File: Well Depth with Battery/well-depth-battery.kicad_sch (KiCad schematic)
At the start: 59 parts, among them J1 Conn_01x02_Female, J2 Conn_01x04_Female, J3 Conn_01x04_Male, J4 Conn_01x02_Male, J5 USB_A, Q1 Q_NMOS_GSD, Q2 Q_PMOS_GSD, Q3 Q_PMOS_GSD, U1 LM358, U2 LM358, U3 TL431DBZ, U4 PCF85263AT, U5 ATSAMD11C14A-SS, U6 MCP1793T-3302H/DC, Y1 Crystal_Small

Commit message: WDB: Floorplanning
Also fixed .gitignore to not ignore lib
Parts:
- removed H4: MountingHole, MountingHole:MountingHole_3.2mm_M3, symbol Mechanical:MountingHole
- J5: footprint Connector_USB:USB_A_Molex_67643_Horizontal -> Connector_USB:USB_A_Molex_105057_Vertical
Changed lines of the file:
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@@
     (pin "2")
-  )
-  (symbol (lib_id "Mechanical:MountingHole") (at 140.97 39.37 0) (unit 1)
-    (in_bom yes) (on_board yes) (fields_autoplaced)
-    (property "Reference" "H4" (id 0) (at 143.51 38.4615 0)
-      (effects (font (size 1.27 1.27)) (justify left))
-    )
-    (property "Value" "MountingHole" (id 1) (at 143.51 41.2366 0)
-      (effects (font (size 1.27 1.27)) (justify left))
-    )
-    (property "Footprint" "MountingHole:MountingHole_3.2mm_M3" (id 2) (at 140.97 39.37 0)
-      (effects (font (size 1.27 1.27)) hide)
-    )
-    (property "Datasheet" "~" (id 3) (at 140.97 39.37 0)
-      (effects (font (size 1.27 1.27)) hide)
-    )
   )
   (symbol (lib_id "Amplifier_Operational:LM358") (at 105.41 151.13 0) (mirror x) (unit 2)
@@
       (effects (font (size 1.27 1.27)) (justify right))
     )
-    (property "Footprint" "Connector_USB:USB_A_Molex_67643_Horizontal" (id 2) (at 144.78 77.47 0)
+    (property "Footprint" "Connector_USB:USB_A_Molex_105057_Vertical" (id 2) (at 144.78 77.47 0)
       (effects (font (size 1.27 1.27)) hide)
     )
@@
       (reference "H3") (unit 1) (value "MountingHole") (footprint "MountingHole:MountingHole_3.2mm_M3")
     )
-    (path "/89c4924b-9262-42f1-a4c5-29cb8a3e67b0"
-      (reference "H4") (unit 1) (value "MountingHole") (footprint "MountingHole:MountingHole_3.2mm_M3")
-    )
     (path "/dd9eb823-0ce6-40ba-88dd-0922cd3c375c"
       (reference "J1") (unit 1) (value "Conn_01x02_Female") (footprint "Connector_PinHeader_2.54mm:PinHeader_1x02_P2.54mm_Vertical")
@@
     )
     (path "/eac5442d-319a-4688-a3db-4a4027c3734b"
-      (reference "J5") (unit 1) (value "USB_A") (footprint "Connector_USB:USB_A_Molex_67643_Horizontal")
+      (reference "J5") (unit 1) (value "USB_A") (footprint "Connector_USB:USB_A_Molex_105057_Vertical")
     )
     (path "/55fe9388-2515-47be-8ff8-75dd7e5bdfd0"

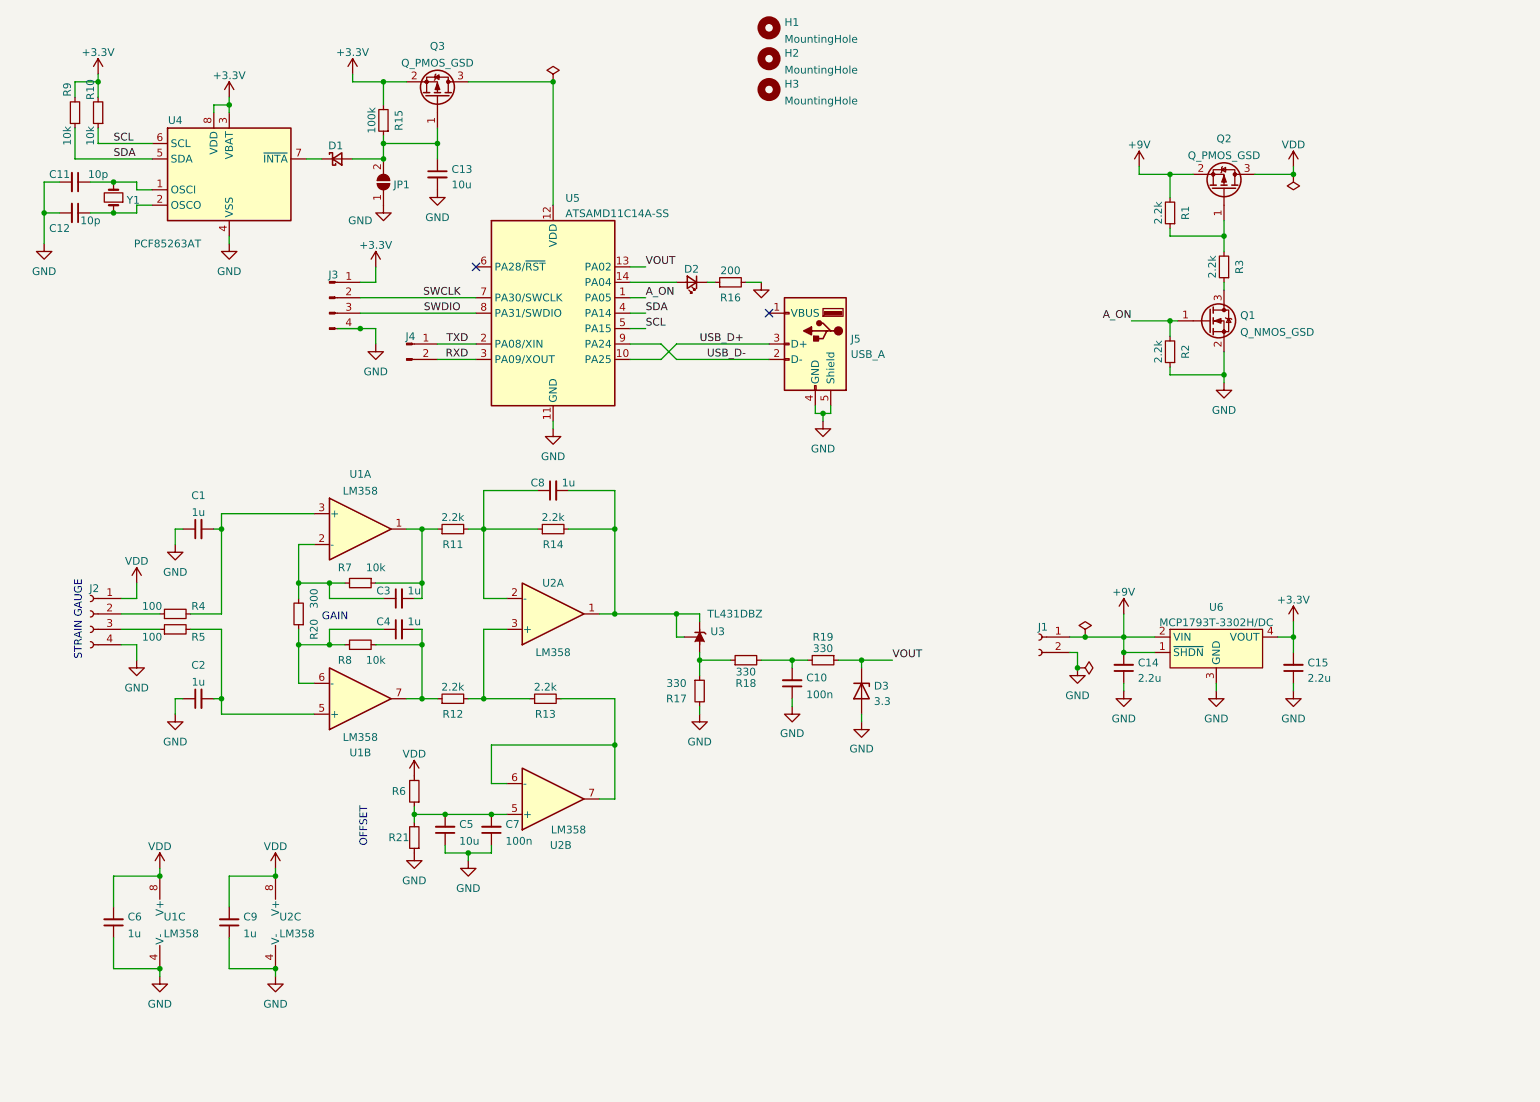
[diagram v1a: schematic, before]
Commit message: Start WDB Refactor w/ SAMD21
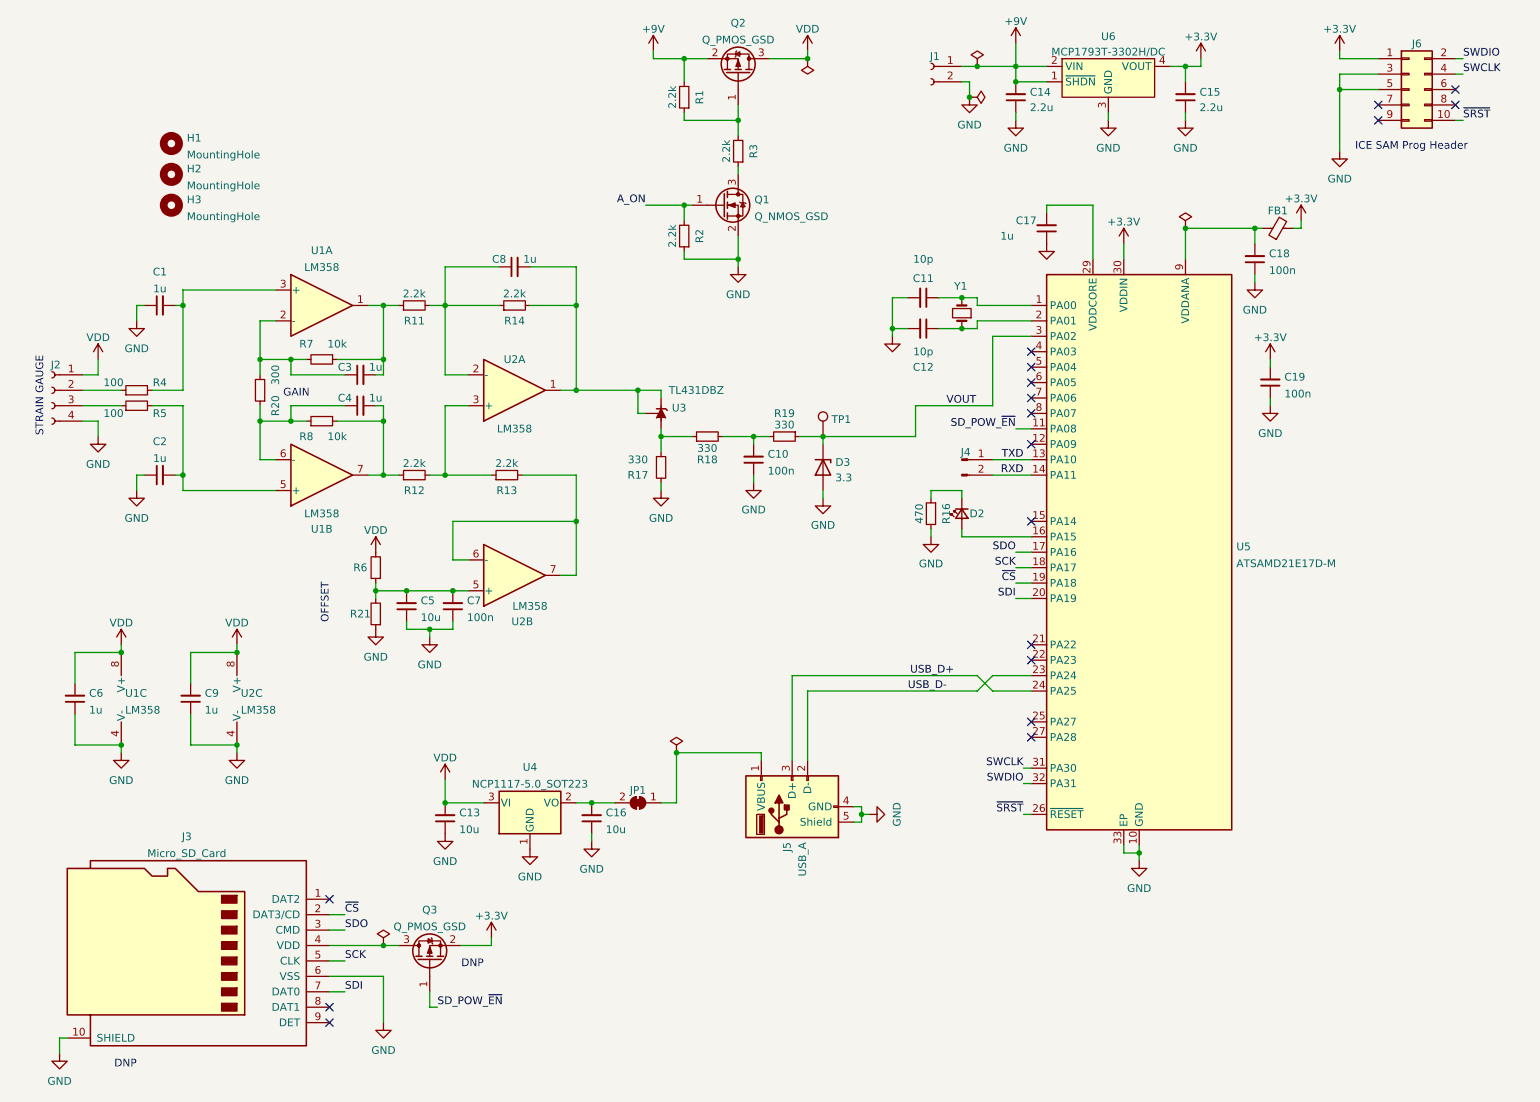
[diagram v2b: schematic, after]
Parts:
- removed D1: D_Schottky_Small, Diode_SMD:D_SOD-323, symbol Device:D_Schottky_Small
- removed J3: Conn_01x04_Male, Connector_PinHeader_2.54mm:PinHeader_1x04_P2.54mm_Vertical, symbol Connector:Conn_01x04_Male
- removed JP1: SolderJumper_2_Open, Resistor_SMD:R_0603_1608Metric, symbol Jumper:SolderJumper_2_Open
- removed R10, R9: 10k, Resistor_SMD:R_0402_1005Metric, symbol Device:R_Small
- removed R15: 100k, Resistor_SMD:R_0402_1005Metric, symbol Device:R_Small
- removed U4: PCF85263AT, Package_SO:SOIC-8_3.9x4.9mm_P1.27mm, symbol Timer_RTC:PCF85263AT
- removed U5: ATSAMD11C14A-SS, Package_SO:SOIC-14_3.9x8.7mm_P1.27mm, symbol MCU_Microchip_SAMD:ATSAMD11C14A-SS
- added C16: 10u, Capacitor_SMD:C_0805_2012Metric, symbol Device:C_Small
- added C17: 1u, Capacitor_SMD:C_0402_1005Metric, symbol Device:C_Small
- added C18, C19: 100n, Capacitor_SMD:C_0402_1005Metric, symbol Device:C_Small
- added FB1: FerriteBead_Small, symbol Device:FerriteBead_Small
- added J3: Micro_SD_Card, EWB:MEM2051-00-195-00-A, symbol well-monitor:Micro_SD_Card
- added J6: Conn_02x05_Odd_Even, symbol Connector_Generic:Conn_02x05_Odd_Even
- added JP1: SolderJumper_2_Bridged, symbol Jumper:SolderJumper_2_Bridged
- added TP1: TestPoint, symbol Connector:TestPoint
- added U4: NCP1117-5.0_SOT223, Package_TO_SOT_SMD:SOT-223-3_TabPin2, symbol Regulator_Linear:NCP1117-5.0_SOT223
- added U5: ATSAMD21E17D-M, Package_DFN_QFN:QFN-32-1EP_5x5mm_P0.5mm_EP3.6x3.6mm, symbol MCU_Microchip_SAMD:ATSAMD21E17D-M
- R16: value 200 -> 470
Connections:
- net +3V3: now also C19.2, FB1.2, J6.1 (Pin_1), U5.30 (VDDIN)
- net GND: now also C13.1, C16.1, C17.1, C18.1, C19.1, J3.10 (SHIELD), J3.6 (VSS), J6.3 (Pin_3), J6.5 (Pin_5), U4.1 (GND), U5.10 (GND), U5.28 (GND), U5.33 (EP); no longer C13.2
- net RXD: now also U5.14 (PA11)
- net SWCLK: now also J6.4 (Pin_4), U5.31 (PA30)
- net SWDIO: now also J6.2 (Pin_2), U5.32 (PA31)
- net TXD: now also U5.13 (PA10)
- net USB_D+: now also U5.24 (PA25)
- net USB_D-: now also U5.23 (PA24)
- net VDD: now also C13.2, U4.3 (VI)
- net VOUT: now also TP1.1, U5.3 (PA02)
- net at C12.1, Y1.1: now also U5.2 (PA01)
- net at C11.1, Y1.2: now also U5.1 (PA00)
- net at Q3.3 (D): now also J3.4 (VDD)
- net at D2.2 (A): now also U5.16 (PA15)
- net SD_POW_~{EN}: now reaches Q3.1 (G)
- net SD_POW_~{EN}: now also U5.11 (PA08); no longer C13.1
- net at J5.1 (VBUS): now also JP1.1 (A)
- new net: C16.2, JP1.2 (B), U4.2 (VO)
- new net: C17.2, U5.29 (VDDCORE)
- new net: C18.2, FB1.1, U5.9 (VDDANA)
- new net SCK: J3.5 (CLK), U5.18 (PA17)
- new net SDI: J3.7 (DAT0), U5.20 (PA19)
- new net SDO: J3.3 (CMD), U5.17 (PA16)
- new net ~{CS}: J3.2 (DAT3/CD), U5.19 (PA18)
- new net ~{SRST}: J6.10 (Pin_10), U5.26 (~{RESET})
- no-connect marks 2 -> 18
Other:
- note added: "DNP"
- note added: "ICE SAM Prog Header"
- moved on the sheet: C1, C10, C11, C12, C14, C15, C2, C3, C4, C5, C6, C7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

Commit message: WDB: ERC Pass
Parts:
- U6: symbol well-monitor:MCP1793T-3302H/DC -> well-monitor:MCP1793T-3302H-DC
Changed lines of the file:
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@@
     (pin "1")
   )
-  (symbol (lib_id "well-monitor:MCP1793T-3302H{slash}DC") (at 196.85 31.75 0) (unit 1)
+  (symbol (lib_id "well-monitor:MCP1793T-3302H-DC") (at 196.85 31.75 0) (unit 1)
     (in_bom yes) (on_board yes) (fields_autoplaced)
     (property "Reference" "U6" (id 0) (at 196.85 25.561 0))

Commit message: WDB: DRC Pass and Fab
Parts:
- removed JP1: SolderJumper_2_Bridged, symbol Jumper:SolderJumper_2_Bridged
- FB1: footprint (none) -> Resistor_SMD:R_0402_1005Metric
- J6: footprint (none) -> EWB:3221-10-0300-00-TR
- TP1: footprint (none) -> TestPoint:TestPoint_THTPad_1.5x1.5mm_Drill0.7mm
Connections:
- net A_ON: now also U5.12 (PA09)
- net at J5.1 (VBUS): now also C16.2, U4.2 (VO)
- no-connect marks 18 -> 17
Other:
- moved on the sheet: C13, C16, U4

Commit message: removed sd card
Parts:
- removed J3: Micro_SD_Card, EWB:MEM2051-00-195-00-A, symbol well-monitor:Micro_SD_Card
- removed Q3: Q_PMOS_GSD, Package_TO_SOT_SMD:SOT-23, symbol Device:Q_PMOS_GSD
- added R? (x2): 100k, Resistor_SMD:R_0402_1005Metric, symbol Device:R_Small
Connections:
- net GND: now also R?.1
- net VDD: now also R?.2
- net at J2.3 (Pin_3), R5.1: now also R?.1, R?.2
- net SCK: no longer names the net of U5.18 (PA17)
- net SDI: no longer names the net of U5.20 (PA19)
- net SDO: no longer names the net of U5.17 (PA16)
- net SD_POW_~{EN}: no longer names the net of U5.11 (PA08)
- net ~{CS}: no longer names the net of U5.19 (PA18)
- no-connect marks 17 -> 19
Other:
- note removed: "DNP"

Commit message: First pass routing for rectangular board
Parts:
- removed J5: USB_A, Connector_USB:USB_A_Molex_105057_Vertical, symbol Connector:USB_A
- removed J6: Conn_02x05_Odd_Even, EWB:3221-10-0300-00-TR, symbol Connector_Generic:Conn_02x05_Odd_Even
- added H4: MountingHole, MountingHole:MountingHole_3.2mm_M3, symbol Mechanical:MountingHole
- added J3: Conn_02x04_Odd_Even, EWB:CardEdge_Prog, symbol Connector_Generic:Conn_02x04_Odd_Even
- added J6: Conn_01x04, Connector_PinHeader_2.54mm:PinHeader_2x02_P2.54mm_Vertical, symbol Connector_Generic:Conn_01x04
- added RV1: 100k, Potentiometer_SMD:Potentiometer_Bourns_3314J_Vertical, symbol Device:R_Potentiometer_Trim
- added RV2: 1k, Potentiometer_SMD:Potentiometer_Bourns_3314J_Vertical, symbol Device:R_Potentiometer_Trim
- gave numbers to parts that had none: 2
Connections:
- net +3V3: now also J3.1 (Pin_1)
- net GND: now also J3.3 (Pin_3), J3.5 (Pin_5), J3.7 (Pin_7), J6.1 (Pin_1), RV1.3
- net SWCLK: now also J3.4 (Pin_4)
- net SWDIO: now also J3.2 (Pin_2)
- net USB_D+: now also J6.3 (Pin_3)
- net USB_D-: now also J6.2 (Pin_2)
- net VDD: now also RV1.1
- net ~{SRST}: now also J3.8 (Pin_8)
- net at C3.1, R20.2, R7.2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: now also RV2.1
- net at C5.2, C7.2, R21.2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: now also RV1.2
- net at C16.2, U4.2 (VO): now also J6.4 (Pin_4)
- net at C4.1, R20.1, R8.1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: now also RV2.2, RV2.3
- no-connect marks 19 -> 16
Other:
- moved on the sheet: H1, H2, H3
